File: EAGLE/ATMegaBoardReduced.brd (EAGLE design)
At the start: 57.1 x 50.5 mm, 17 parts, among them IC2 ATMEGA168-20P, IC3 REG1117, X1 49S/18PF

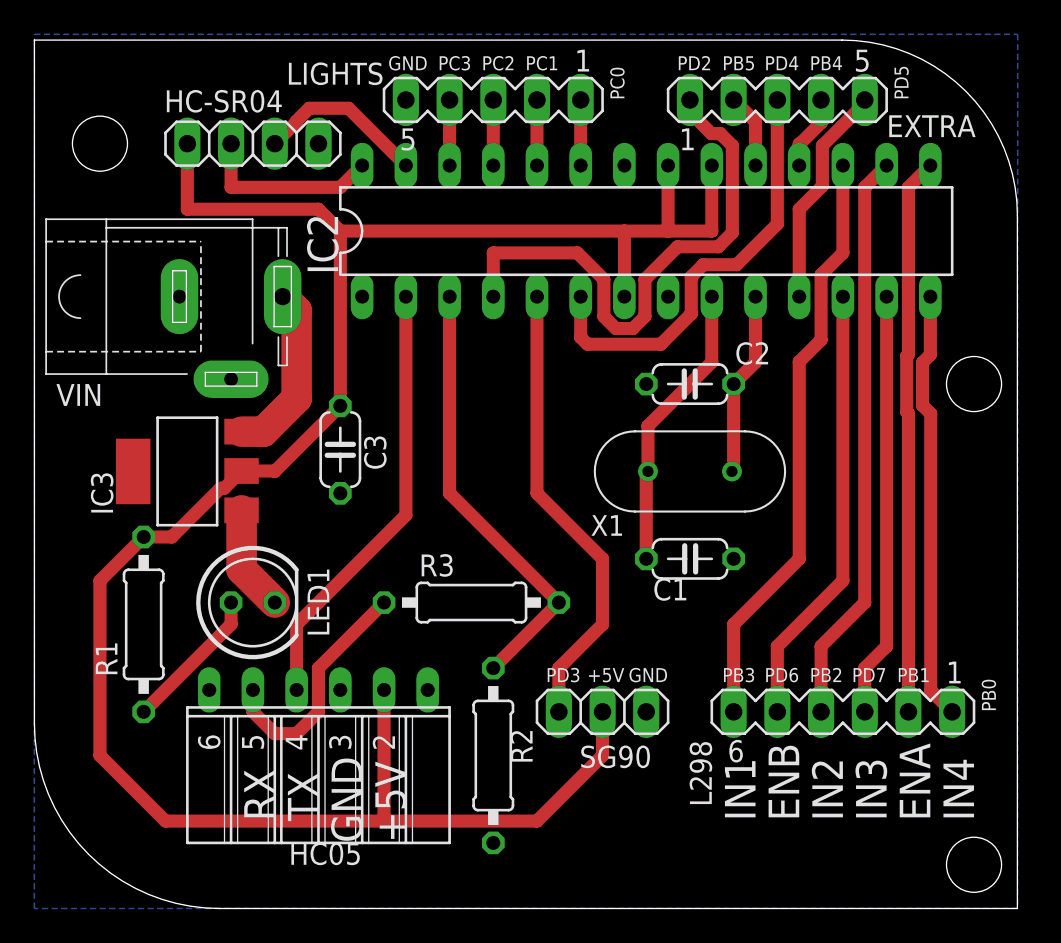
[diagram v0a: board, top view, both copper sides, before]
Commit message: updated layout
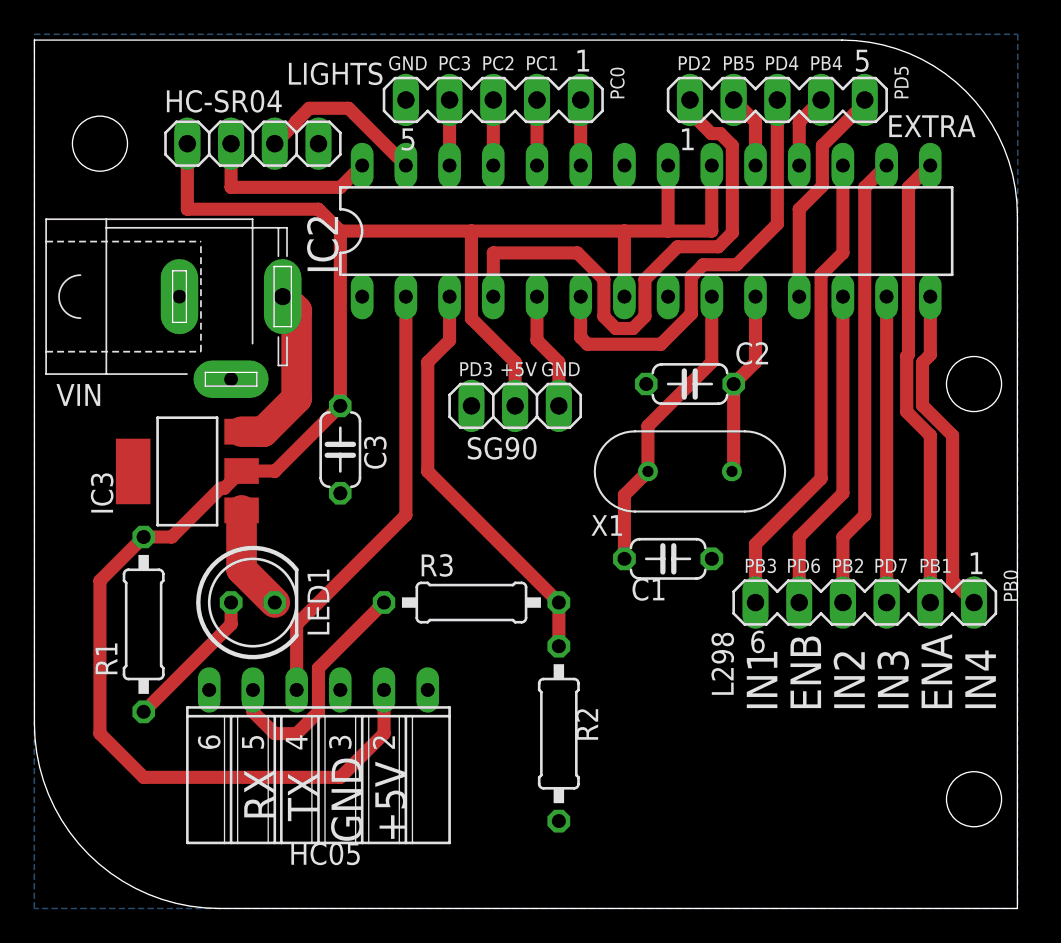
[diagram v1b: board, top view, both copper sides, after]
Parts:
- moved SG90 18.5 mm to (39.4, 34.3), turned to 180 degrees
- moved L298 6.48 mm to (59.7, 22.9)
- moved R2 4.02 mm to (41.9, 15.2)
- moved C1 1.27 mm to (48.3, 25.4)
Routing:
- net 9GPWM: track 26.8 -> 6.88 mm
- net +5V: track 127.3 -> 115.9 mm
- net IN1: track 34.4 -> 27.5 mm
- net IN3: track 24.7 -> 17.8 mm
- net ENB: track 25.7 -> 18.8 mm
- net IN2: track 33.3 -> 26.5 mm
- net ENA: track 32.4 -> 26.5 mm
- net IN4: track 25.0 -> 19.2 mm
- net RX: track 25.8 -> 24.0 mm
- net PB4: track 5.63 -> 4.34 mm
- net XTAL1: track 16.8 -> 17.3 mm

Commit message: minor layout changes
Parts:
- moved C3 1.27 mm to (30.5, 31.8)
- moved VIN 1.27 mm to (24.1, 40.6)
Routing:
- net +5V: track 115.9 -> 126.7 mm
- net VIN: track 10.3 -> 11.5 mm
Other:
- board size 57.1 x 50.5 mm -> 55.9 x 50.5 mm
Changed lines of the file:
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@@
 <board>
 <plain>
-<wire x1="58.37200625" y1="55.55" x2="11.43" y2="55.55" width="0" layer="20"/>
-<wire x1="11.43" y1="55.55" x2="11.43" y2="15.8294" width="0" layer="20"/>
-<wire x1="11.43" y1="15.8294" x2="22.1794" y2="5.08" width="0" layer="20" curve="90"/>
+<wire x1="58.37200625" y1="55.55" x2="12.7" y2="55.55" width="0" layer="20"/>
+<wire x1="12.7" y1="55.55" x2="12.7" y2="15.8294" width="0" layer="20"/>
+<wire x1="12.7" y1="15.8294" x2="22.1794" y2="5.08" width="0" layer="20" curve="90"/>
 <wire x1="22.1794" y1="5.08" x2="68.56" y2="5.08" width="0" layer="20"/>
 <wire x1="68.56" y1="5.08" x2="68.56" y2="45.36200625" width="0" layer="20"/>
@@
 <text x="62.23" y="25.4" size="0.8128" layer="21" rot="R180">PD7</text>
 <text x="64.77" y="25.4" size="0.8128" layer="21" rot="R180">PB1</text>
-<text x="68.58" y="22.86" size="0.8128" layer="21" rot="R90">PB0</text>
+<text x="67.31" y="25.4" size="0.8128" layer="21" rot="R270">PB0</text>
 </plain>
 <attributes>
@@
 </element>
 <element name="IC2" library="adafruit" package="DIL28-3" value="ATMEGA168-20P" x="46.99" y="44.45" smashed="yes">
-<attribute name="NAME" x="29.083" y="41.91" size="1.778" layer="25" ratio="10" rot="R90"/>
+<attribute name="NAME" x="67.183" y="41.91" size="1.778" layer="25" ratio="10" rot="R90"/>
 <attribute name="VALUE" x="31.242" y="43.5102" size="1.778" layer="27" ratio="10"/>
 </element>
@@
 <attribute name="VALUE" x="26.162" y="27.686" size="1.27" layer="27" ratio="10" rot="R90"/>
 </element>
-<element name="C3" library="rcl" library_urn="urn:adsk.eagle:library:334" package="C050-024X044" package3d_urn="urn:adsk.eagle:package:23643/1" value="220uF" x="29.21" y="31.75" smashed="yes" rot="R270">
-<attribute name="NAME" x="30.607" y="32.639" size="1.27" layer="25" ratio="10" rot="R270"/>
-<attribute name="POPULARITY" value="14" x="29.21" y="31.75" size="1.778" layer="27" rot="R270" display="off"/>
-<attribute name="SPICEPREFIX" value="C" x="29.21" y="31.75" size="1.778" layer="27" rot="R270" display="off"/>
-<attribute name="VALUE" x="26.543" y="33.909" size="1.27" layer="27" ratio="10" rot="R270"/>
+<element name="C3" library="rcl" library_urn="urn:adsk.eagle:library:334" package="C050-024X044" package3d_urn="urn:adsk.eagle:package:23643/1" value="220uF" x="30.48" y="31.75" smashed="yes" rot="R270">
+<attribute name="NAME" x="31.877" y="32.639" size="1.27" layer="25" ratio="10" rot="R270"/>
+<attribute name="POPULARITY" value="14" x="30.48" y="31.75" size="1.778" layer="27" rot="R270" display="off"/>
+<attribute name="SPICEPREFIX" value="C" x="30.48" y="31.75" size="1.778" layer="27" rot="R270" display="off"/>
+<attribute name="VALUE" x="27.813" y="33.909" size="1.27" layer="27" ratio="10" rot="R270"/>
 </element>
 <element name="R1" library="rcl" library_urn="urn:adsk.eagle:library:334" package="0207/10" package3d_urn="urn:adsk.eagle:package:23491/2" value="1k" x="17.78" y="21.59" smashed="yes" rot="R90">
@@
 <attribute name="VALUE" x="27.3304" y="21.0566" size="1.27" layer="27" ratio="10"/>
 </element>
-<element name="VIN" library="con-jack" library_urn="urn:adsk.eagle:library:154" package="SPC4078" package3d_urn="urn:adsk.eagle:package:7494/1" value="" x="22.86" y="40.64" smashed="yes">
-<attribute name="MF" value="" x="22.86" y="40.64" size="1.778" layer="27" display="off"/>
-<attribute name="MPN" value="" x="22.86" y="40.64" size="1.778" layer="27" display="off"/>
-<attribute name="NAME" x="12.7" y="34.29" size="1.27" layer="25"/>
-<attribute name="OC_FARNELL" value="unknown" x="22.86" y="40.64" size="1.778" layer="27" display="off"/>
-<attribute name="OC_NEWARK" value="unknown" x="22.86" y="40.64" size="1.778" layer="27" display="off"/>
-<attribute name="POPULARITY" value="3" x="22.86" y="40.64" size="1.778" layer="27" display="off"/>
-<attribute name="VALUE" x="12.7" y="34.29" size="1.27" layer="27"/>
+<element name="VIN" library="con-jack" library_urn="urn:adsk.eagle:library:154" package="SPC4078" package3d_urn="urn:adsk.eagle:package:7494/1" value="" x="24.13" y="40.64" smashed="yes">
+<attribute name="MF" value="" x="24.13" y="40.64" size="1.778" layer="27" display="off"/>
+<attribute name="MPN" value="" x="24.13" y="40.64" size="1.778" layer="27" display="off"/>
+<attribute name="NAME" x="13.97" y="34.29" size="1.27" layer="25"/>
+<attribute name="OC_FARNELL" value="unknown" x="24.13" y="40.64" size="1.778" layer="27" display="off"/>
+<attribute name="OC_NEWARK" value="unknown" x="24.13" y="40.64" size="1.778" layer="27" display="off"/>
+<attribute name="POPULARITY" value="3" x="24.13" y="40.64" size="1.778" layer="27" display="off"/>
+<attribute name="VALUE" x="13.97" y="34.29" size="1.27" layer="27"/>
 </element>
 <element name="R2" library="rcl" library_urn="urn:adsk.eagle:library:334" package="0207/10" package3d_urn="urn:adsk.eagle:package:23491/2" value="2k" x="41.91" y="15.24" smashed="yes" rot="R90">
@@
 <contactref element="R1" pad="2"/>
 <contactref element="HC05" pad="2"/>
-<wire x1="25.4" y1="30.48" x2="29.21" y2="34.29" width="0.762" layer="1"/>
-<wire x1="29.21" y1="34.29" x2="29.21" y2="44.45" width="0.762" layer="1"/>
-<wire x1="29.21" y1="44.45" x2="36.83" y2="44.45" width="0.762" layer="1"/>
+<wire x1="36.83" y1="44.45" x2="20.32" y2="44.45" width="0.762" layer="1"/>
 <wire x1="36.83" y1="44.45" x2="45.72" y2="44.45" width="0.762" layer="1"/>
 <wire x1="45.72" y1="44.45" x2="48.26" y2="44.45" width="0.762" layer="1"/>
@@
 <wire x1="17.78" y1="12.7" x2="29.21" y2="12.7" width="0.762" layer="1"/>
 <wire x1="31.75" y1="15.24" x2="31.75" y2="17.78" width="0.762" layer="1"/>
-<wire x1="27.94" y1="45.72" x2="20.32" y2="45.72" width="0.762" layer="1"/>
-<wire x1="20.32" y1="45.72" x2="20.32" y2="49.53" width="0.762" layer="1"/>
-<wire x1="29.21" y1="44.45" x2="27.94" y2="45.72" width="0.762" layer="1"/>
 <wire x1="17.78" y1="12.7" x2="15.24" y2="15.24" width="0.762" layer="1"/>
 <wire x1="23.4696" y1="30.5054" x2="22.4663" y2="29.5021" width="0.762" layer="1"/>
@@
 <wire x1="22.24535625" y1="29.5021" x2="19.41325625" y2="26.67" width="0.762" layer="1"/>
 <wire x1="19.41325625" y1="26.67" x2="17.78" y2="26.67" width="0.762" layer="1"/>
-<wire x1="23.4696" y1="30.5054" x2="25.3746" y2="30.5054" width="0.762" layer="1"/>
-<wire x1="25.3746" y1="30.5054" x2="25.4" y2="30.48" width="0.762" layer="1"/>
+<wire x1="23.4696" y1="30.5054" x2="26.6446" y2="30.5054" width="0.762" layer="1"/>
+<wire x1="26.6446" y1="30.5054" x2="26.67" y2="30.48" width="0.762" layer="1"/>
 <wire x1="36.83" y1="44.45" x2="36.83" y2="39.37" width="0.762" layer="1"/>
 <wire x1="39.37" y1="34.29" x2="39.37" y2="36.83" width="0.762" layer="1"/>
 <wire x1="39.37" y1="36.83" x2="36.83" y2="39.37" width="0.762" layer="1"/>
 <wire x1="29.21" y1="12.7" x2="31.75" y2="15.24" width="0.762" layer="1"/>
+<wire x1="26.6446" y1="30.5054" x2="26.6954" y2="30.5054" width="0.762" layer="1"/>
+<wire x1="26.6954" y1="30.5054" x2="30.48" y2="34.29" width="0.762" layer="1"/>
+<wire x1="23.4696" y1="30.5054" x2="23.4442" y2="30.48" width="0.762" layer="1"/>
+<wire x1="23.4442" y1="30.48" x2="20.32" y2="30.48" width="0.762" layer="1"/>
+<wire x1="20.32" y1="30.48" x2="19.05" y2="31.75" width="0.762" layer="1"/>
+<wire x1="19.05" y1="31.75" x2="19.05" y2="44.45" width="0.762" layer="1"/>
+<wire x1="20.32" y1="44.45" x2="19.05" y2="44.45" width="0.762" layer="1"/>
+<wire x1="20.32" y1="49.53" x2="20.32" y2="44.45" width="0.762" layer="1"/>
 </signal>
 <signal name="GND" class="1">
@@
 <contactref element="R2" pad="1"/>
 <polygon width="0.1524" layer="16">
-<vertex x="11.43" y="5.08"/>
-<vertex x="11.43" y="55.88"/>
+<vertex x="12.7" y="5.08"/>
+<vertex x="12.7" y="55.88"/>
 <vertex x="68.58" y="55.88"/>
 <vertex x="68.58" y="5.08"/>
@@
 <contactref element="IC3" pad="3"/>
 <contactref element="VIN" pad="3"/>
-<wire x1="25.86" y1="40.64" x2="26.67" y2="39.83" width="1.778" layer="1"/>
-<wire x1="26.67" y1="34.7218" x2="24.7396" y2="32.7914" width="1.778" layer="1"/>
-<wire x1="24.7396" y1="32.7914" x2="23.4696" y2="32.7914" width="1.778" layer="1"/>
-<wire x1="26.67" y1="39.83" x2="26.67" y2="34.7218" width="1.778" layer="1"/>
+<wire x1="27.94" y1="34.7218" x2="26.0096" y2="32.7914" width="1.778" layer="1"/>
+<wire x1="26.0096" y1="32.7914" x2="23.4696" y2="32.7914" width="1.778" layer="1"/>
+<wire x1="27.13" y1="40.64" x2="27.94" y2="39.83" width="1.778" layer="1"/>
+<wire x1="27.94" y1="39.83" x2="27.94" y2="34.7218" width="1.778" layer="1"/>
 </signal>
 <signal name="IN4">

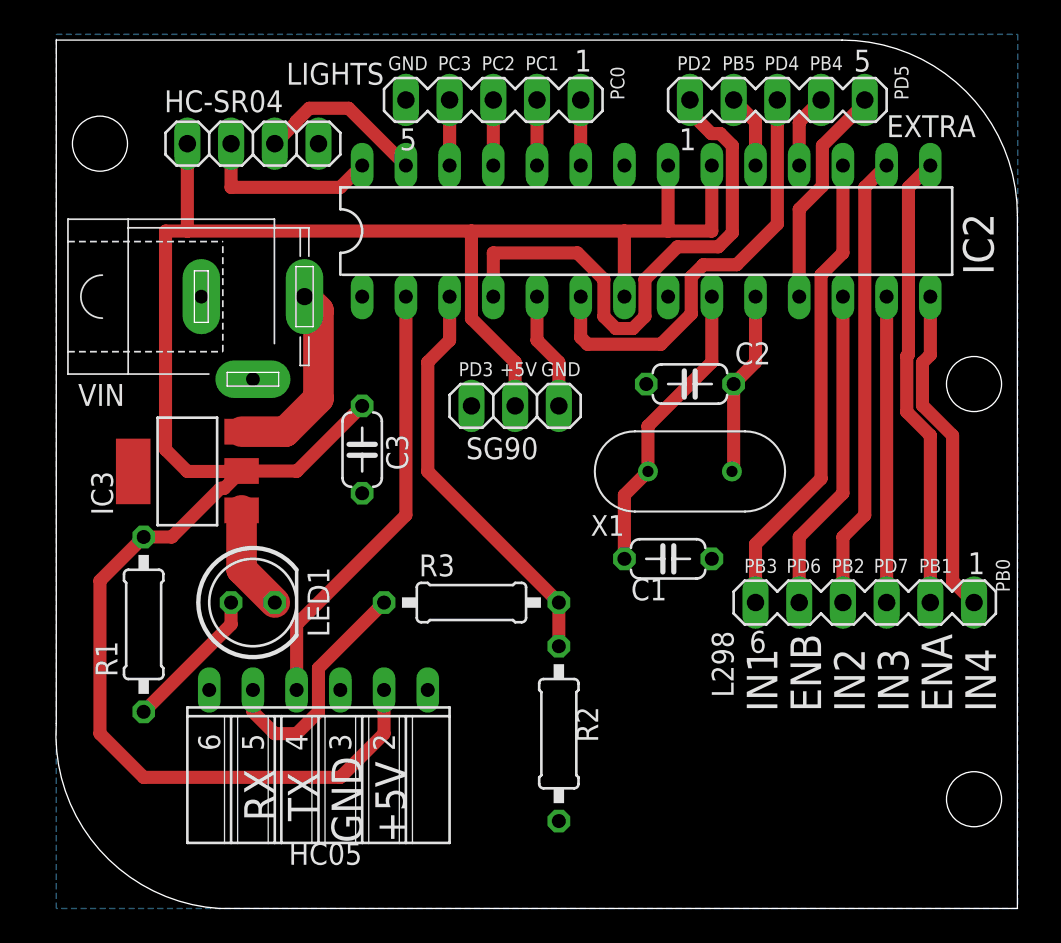
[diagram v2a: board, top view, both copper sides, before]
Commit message: set reset pin high added ground pins
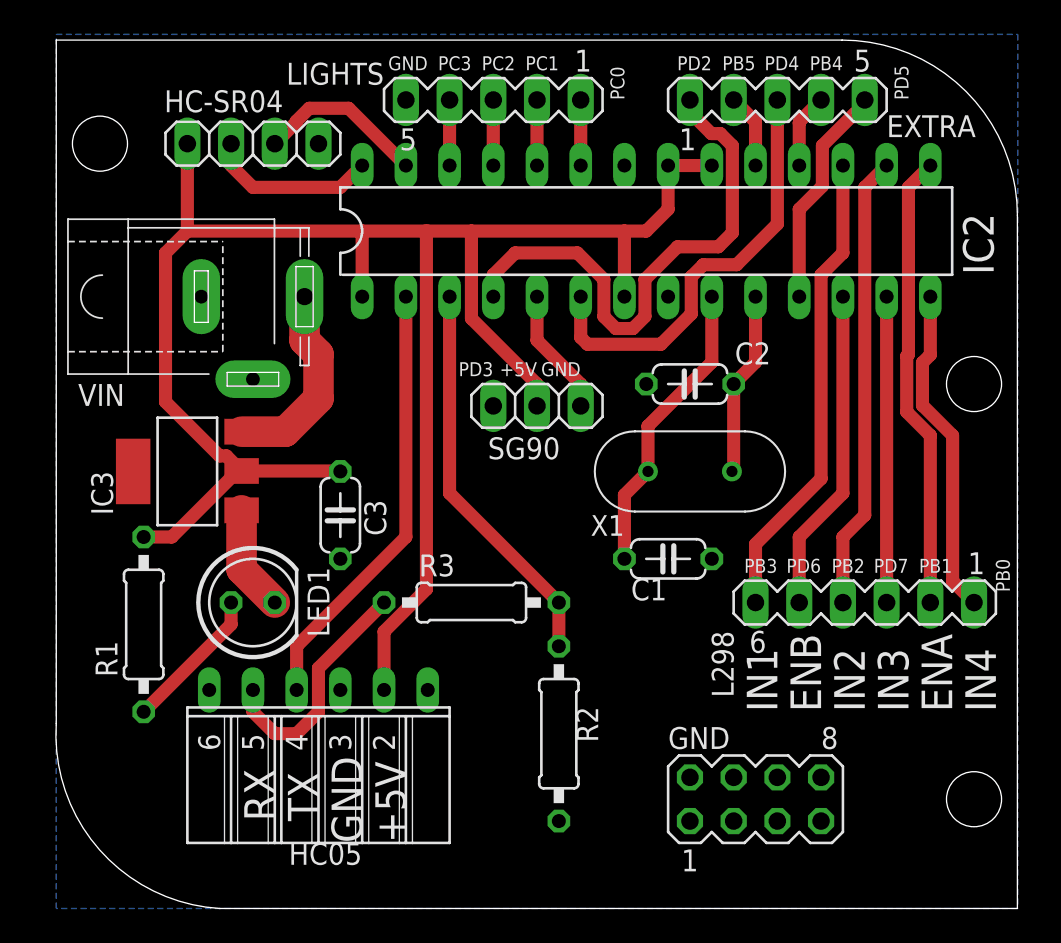
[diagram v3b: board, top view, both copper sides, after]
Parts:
- added GND: (no value), con-lstb:MA04-2
- moved C3 4.02 mm to (29.2, 27.9)
- moved SG90 1.27 mm to (40.6, 34.3)
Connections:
- net +5V: now also IC2.1
- net GND: now also GND.1, GND.2, GND.3, GND.4, GND.5, GND.6, GND.7, GND.8
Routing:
- net +5V: track 126.7 -> 115.2 mm
- net RX: track 24.0 -> 23.0 mm
- net PD2: track 32.1 -> 31.4 mm
- net TRIG: track 10.7 -> 9.94 mm
- net 9GPWM: track 6.88 -> 7.40 mm

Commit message: shifted HC-SR04 away from ATMega
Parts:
- moved HC-SR04 1.80 mm to (22.9, 50.8)
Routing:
- net ECHO: track 9.88 -> 12.4 mm
- net +5V: track 115.2 -> 117.2 mm
- net TRIG: track 9.94 -> 10.7 mm
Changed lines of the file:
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@@
 <attribute name="VALUE" x="51.689" y="36.957" size="1.27" layer="27" ratio="10" rot="R180"/>
 </element>
-<element name="HC-SR04" library="pinhead" library_urn="urn:adsk.eagle:library:325" package="1X04" package3d_urn="urn:adsk.eagle:package:22407/2" value="" x="24.13" y="49.53" smashed="yes">
-<attribute name="NAME" x="18.9738" y="51.3588" size="1.27" layer="25" ratio="10"/>
-<attribute name="POPULARITY" value="91" x="43.18" y="7.62" size="1.778" layer="27" display="off"/>
-<attribute name="VALUE" x="19.05" y="46.355" size="1.27" layer="27"/>
+<element name="HC-SR04" library="pinhead" library_urn="urn:adsk.eagle:library:325" package="1X04" package3d_urn="urn:adsk.eagle:package:22407/2" value="" x="22.86" y="50.8" smashed="yes">
+<attribute name="NAME" x="17.7038" y="52.6288" size="1.27" layer="25" ratio="10"/>
+<attribute name="POPULARITY" value="91" x="41.91" y="8.89" size="1.778" layer="27" display="off"/>
+<attribute name="VALUE" x="17.78" y="47.625" size="1.27" layer="27"/>
 </element>
 <element name="IC2" library="adafruit" package="DIL28-3" value="ATMEGA168-20P" x="46.99" y="44.45" smashed="yes">
@@
 <wire x1="40.64" y1="34.29" x2="40.64" y2="35.56" width="0.762" layer="1"/>
 <wire x1="40.64" y1="35.56" x2="36.83" y2="39.37" width="0.762" layer="1"/>
-<wire x1="20.32" y1="49.53" x2="20.32" y2="44.45" width="0.762" layer="1"/>
+<wire x1="19.05" y1="50.8" x2="19.05" y2="44.45" width="0.762" layer="1"/>
 <wire x1="31.75" y1="17.78" x2="31.75" y2="21.17170625" width="0.762" layer="1"/>
 <wire x1="31.75" y1="21.17170625" x2="34.2138" y2="23.63550625" width="0.762" layer="1"/>
@@
 <wire x1="22.5933" y1="31.3817" x2="22.19275625" y2="31.3817" width="0.762" layer="1"/>
 <wire x1="22.19275625" y1="31.3817" x2="19.05" y2="34.52445625" width="0.762" layer="1"/>
-<wire x1="19.05" y1="34.52445625" x2="19.05" y2="43.18" width="0.762" layer="1"/>
-<wire x1="19.05" y1="43.18" x2="20.32" y2="44.45" width="0.762" layer="1"/>
-<wire x1="20.32" y1="44.45" x2="30.48" y2="44.45" width="0.762" layer="1"/>
+<wire x1="19.05" y1="34.52445625" x2="19.05" y2="44.45" width="0.762" layer="1"/>
+<wire x1="19.05" y1="44.45" x2="30.48" y2="44.45" width="0.762" layer="1"/>
 <wire x1="30.48" y1="44.45" x2="34.1376" y2="44.45" width="0.762" layer="1"/>
 <wire x1="36.83" y1="44.45" x2="45.72" y2="44.45" width="0.762" layer="1"/>
@@
 <contactref element="HC-SR04" pad="3"/>
 <contactref element="IC2" pad="27"/>
-<wire x1="26.6446" y1="50.828575" x2="27.403425" y2="51.5874" width="0.762" layer="1"/>
-<wire x1="25.4" y1="49.53" x2="26.6446" y2="50.7746" width="0.762" layer="1"/>
-<wire x1="26.6446" y1="50.7746" x2="26.6446" y2="50.828575" width="0.762" layer="1"/>
-<wire x1="27.403425" y1="51.5874" x2="29.6926" y2="51.5874" width="0.762" layer="1"/>
-<wire x1="29.6926" y1="51.5874" x2="33.02" y2="48.26" width="0.762" layer="1"/>
+<wire x1="28.4226" y1="52.8574" x2="24.9174" y2="52.8574" width="0.762" layer="1"/>
+<wire x1="24.13" y1="50.8" x2="24.13" y2="52.07" width="0.762" layer="1"/>
+<wire x1="24.9174" y1="52.8574" x2="24.13" y2="52.07" width="0.762" layer="1"/>
+<wire x1="28.4226" y1="52.8574" x2="33.02" y2="48.26" width="0.762" layer="1"/>
 </signal>
 <signal name="TRIG">
 <contactref element="HC-SR04" pad="2"/>
 <contactref element="IC2" pad="28"/>
-<wire x1="22.86" y1="48.26" x2="22.86" y2="49.53" width="0.762" layer="1"/>
-<wire x1="30.48" y1="48.26" x2="29.21" y2="46.99" width="0.762" layer="1"/>
-<wire x1="24.13" y1="46.99" x2="22.86" y2="48.26" width="0.762" layer="1"/>
-<wire x1="29.21" y1="46.99" x2="24.13" y2="46.99" width="0.762" layer="1"/>
+<wire x1="21.59" y1="50.8" x2="21.59" y2="49.53" width="0.762" layer="1"/>
+<wire x1="22.86" y1="48.26" x2="21.59" y2="49.53" width="0.762" layer="1"/>
+<wire x1="30.48" y1="48.26" x2="22.86" y2="48.26" width="0.762" layer="1"/>
 </signal>
 <signal name="9GPWM">
